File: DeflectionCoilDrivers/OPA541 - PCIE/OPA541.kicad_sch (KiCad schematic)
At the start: 31 parts, among them J1 Conn_01x06_Socket, J2 Conn_Coaxial_Small, J3 Conn_Coaxial_Small, J4 Conn_Coaxial_Small, U1 OPA541AP

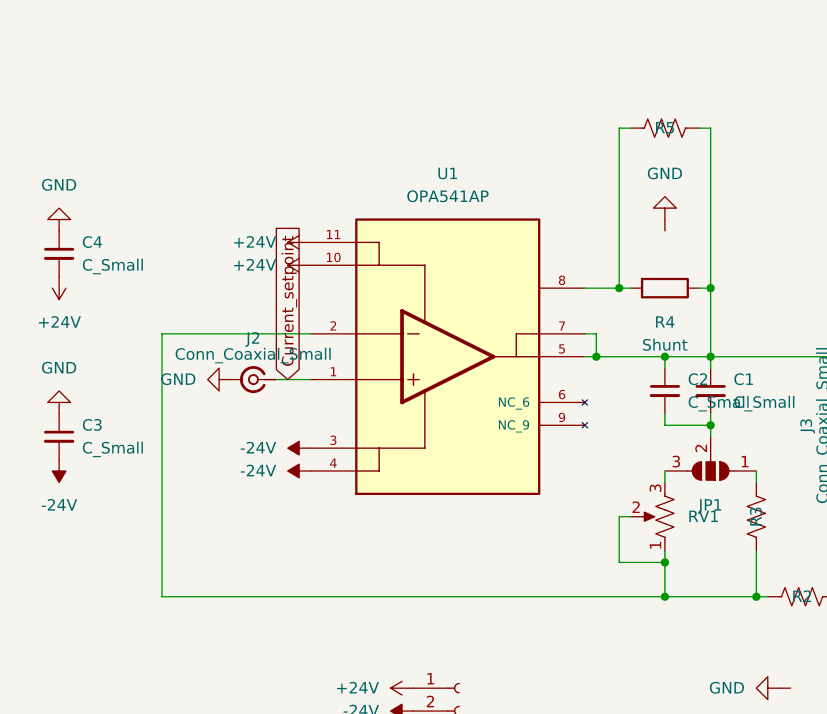
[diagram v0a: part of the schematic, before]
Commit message: opa541 footprint update
moved opa541 footprint from snapmatic to kicad and custom symbol
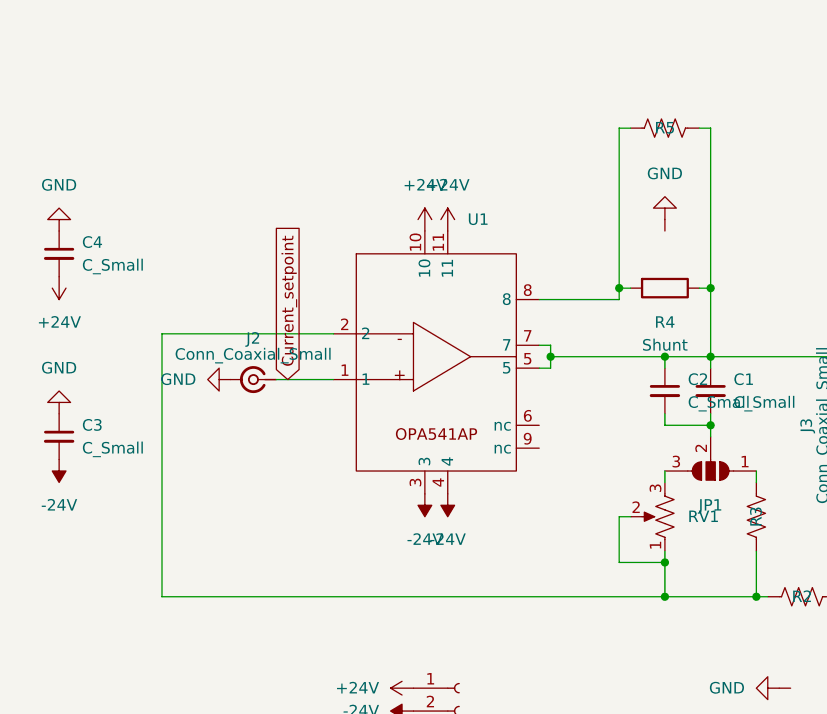
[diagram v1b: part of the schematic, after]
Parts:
- removed U1: OPA541AP, Library:TO170P2027X462X2456-11, symbol OPA541AP:OPA541AP
- added U1: ~, Package_TO_SOT_THT:TO-220-11_P3.4x5.08mm_StaggerOdd_Lead4.85mm_Vertical, symbol New_Library:OPA541
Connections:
- net +24V: now also U1.10, U1.11
- net -24V: now also U1.3, U1.4
- net Current_setpoint: now also U1.1
- net at C1.1, C2.1, J3.1 (In)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: now also U1.5, U1.7
- net at R2.1, R3.2, RV1.1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: now also U1.2
- net at R4.2, R5.1: now also U1.8

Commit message: minor changes
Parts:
- added R8: 1k, Capacitor_THT:C_Disc_D6.0mm_W2.5mm_P5.00mm, symbol Device:R_US
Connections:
- net at R2.1, R3.2, RV1.1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: now also R8.1
- net at J3.2 (Ext), J4.1 (In), R1.1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: now also R8.2
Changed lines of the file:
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@@
 (kicad_sch
-	(version 20231120)
+	(version 20250114)
 	(generator "eeschema")
-	(generator_version "8.0")
+	(generator_version "9.0")
 	(paper "A2")
 	(junction
@@
 	)
 	(junction
+		(at 227.33 173.99)
+		(diameter 0)
+		(color 0 0 0 0)
+	)
+	(junction
 		(at 194.31 143.51)
 		(diameter 0)
@@
 	(wire
 		(pts
+			(xy 218.44 173.99) (xy 217.17 173.99)
+		)
+		(stroke
+			(width 0)
+			(type default)
+		)
+	)
+	(wire
+		(pts
 			(xy 139.7 200.66) (xy 147.32 200.66)
 		)
@@
 	(wire
 		(pts
+			(xy 226.06 173.99) (xy 227.33 173.99)
+		)
+		(stroke
+			(width 0)
+			(type default)
+		)
+	)
+	(wire
+		(pts
 			(xy 144.78 203.2) (xy 147.32 203.2)
 		)
@@
 	(wire
 		(pts
+			(xy 217.17 173.99) (xy 217.17 170.18)
+		)
+		(stroke
+			(width 0)
+			(type default)
+		)
+	)
+	(wire
+		(pts
 			(xy 147.32 205.74) (xy 147.32 203.2)
 		)
@@
 	(wire
 		(pts
+			(xy 227.33 173.99) (xy 227.33 176.53)
+		)
+		(stroke
+			(width 0)
+			(type default)
+		)
+	)
+	(wire
+		(pts
 			(xy 227.33 184.15) (xy 227.33 186.69)
 		)
@@
 	(wire
 		(pts
-			(xy 227.33 170.18) (xy 227.33 176.53)
+			(xy 227.33 170.18) (xy 227.33 173.99)
 		)
 		(stroke
@@
 	)
 	(symbol
+		(lib_id "Device:R_US")
+		(at 222.25 173.99 90)
+		(unit 1)
+		(exclude_from_sim no)
+		(in_bom yes)
+		(on_board yes)
+		(dnp no)
+		(property "Reference" "R8"
+			(at 222.25 173.99 90)
+			(effects
+				(font
+					(size 1.27 1.27)
+				)
+			)
+		)
+		(property "Value" "1k"
+			(at 222.25 170.18 90)
+			(effects
+				(font
+					(size 1.27 1.27)
+				)
+				(hide yes)
+			)
+		)
+		(property "Footprint" "Capacitor_THT:C_Disc_D6.0mm_W2.5mm_P5.00mm"
+			(at 222.504 172.974 90)
+			(effects
+				(font
+					(size 1.27 1.27)
+				)
+				(hide yes)
+			)
+		)
+		(property "Datasheet" "CPF0603F100KC1"
+			(at 222.25 173.99 0)
+			(effects
+				(font
+					(size 1.27 1.27)
+				)
+				(hide yes)
+			)
+		)
+		(property "Description" ""
+			(at 222.25 173.99 0)
+			(effects
+				(font
+					(size 1.27 1.27)
+				)
+				(hide yes)
+			)
+		)
+		(pin "1"
+		)
+		(pin "2"
+		)
+		(instances
+			(project "OPA541"
+				(path "/4509510e-bfdb-428c-8f4b-2027be68d1bf"
+					(reference "R8")
+					(unit 1)
+				)
+			)
+		)
+	)
+	(symbol
 		(lib_id "Device:C_Small")
 		(at 207.01 147.32 0)
@@
 		)
 	)
+	(embedded_fonts no)
 )
